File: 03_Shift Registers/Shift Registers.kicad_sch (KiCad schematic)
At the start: 5 parts, among them J1 Data bus, J2 Alu-X bus, J3 Alu-Y bus, J4 Input 1, J5 Input 2

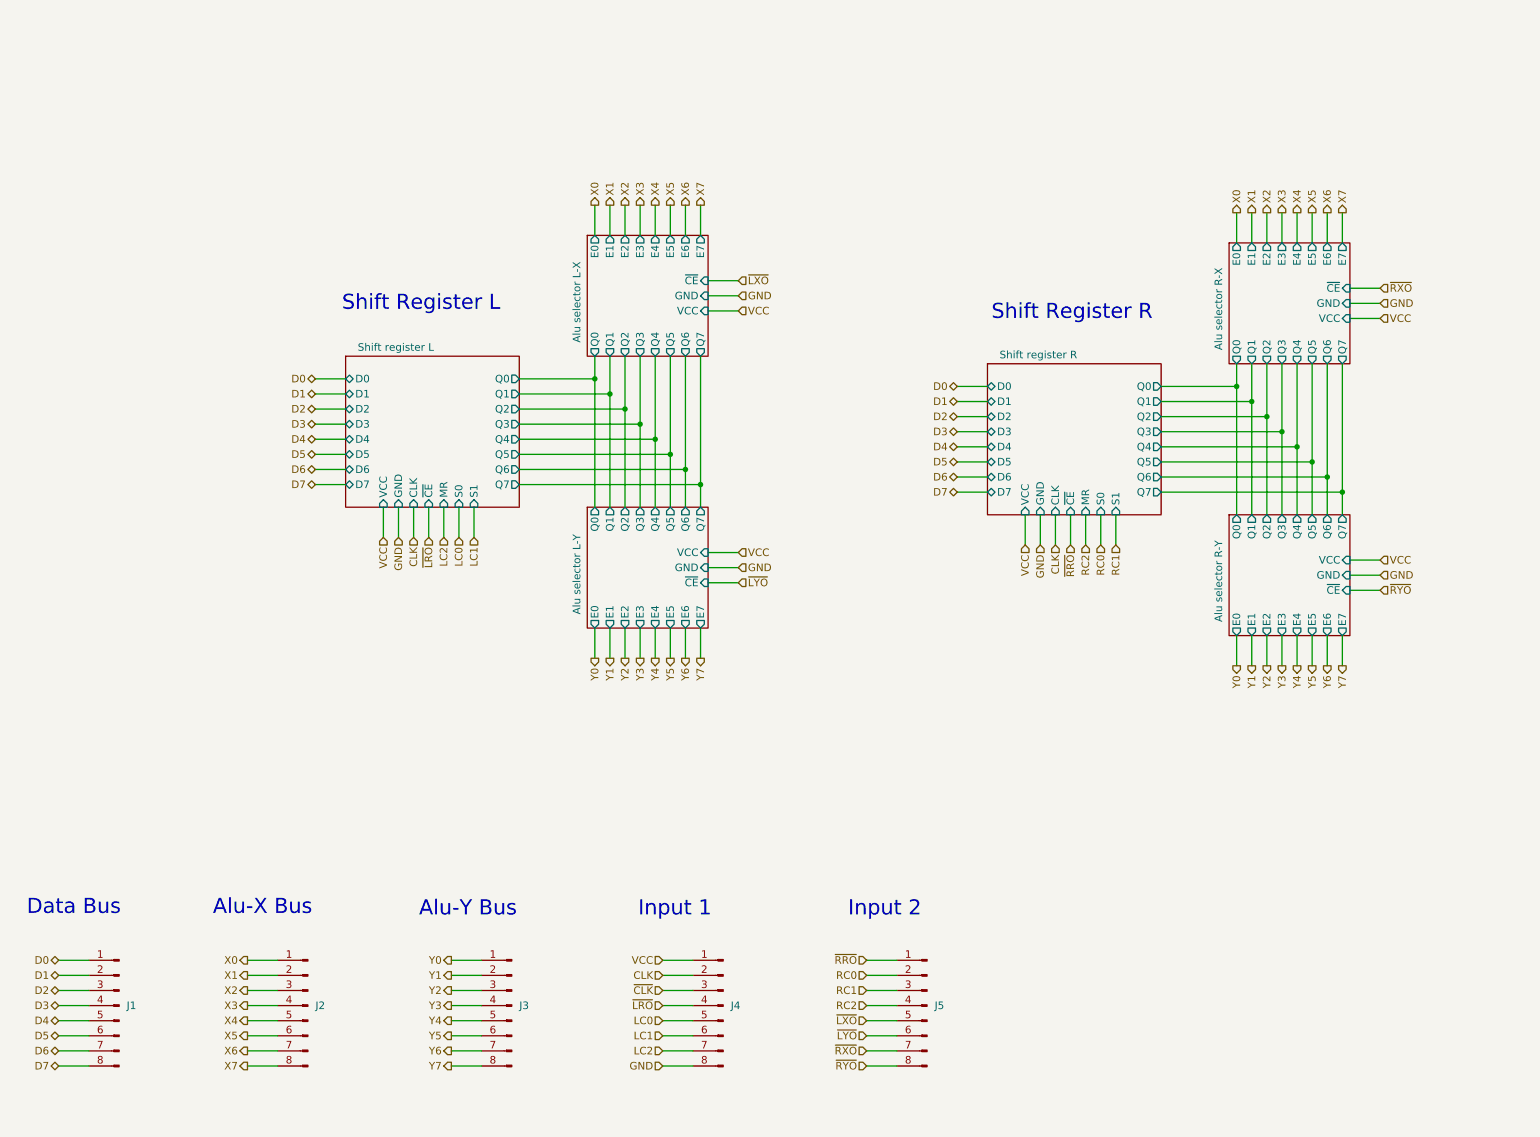
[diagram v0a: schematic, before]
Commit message: Alu control and modules completed, as well as Stack pointer module
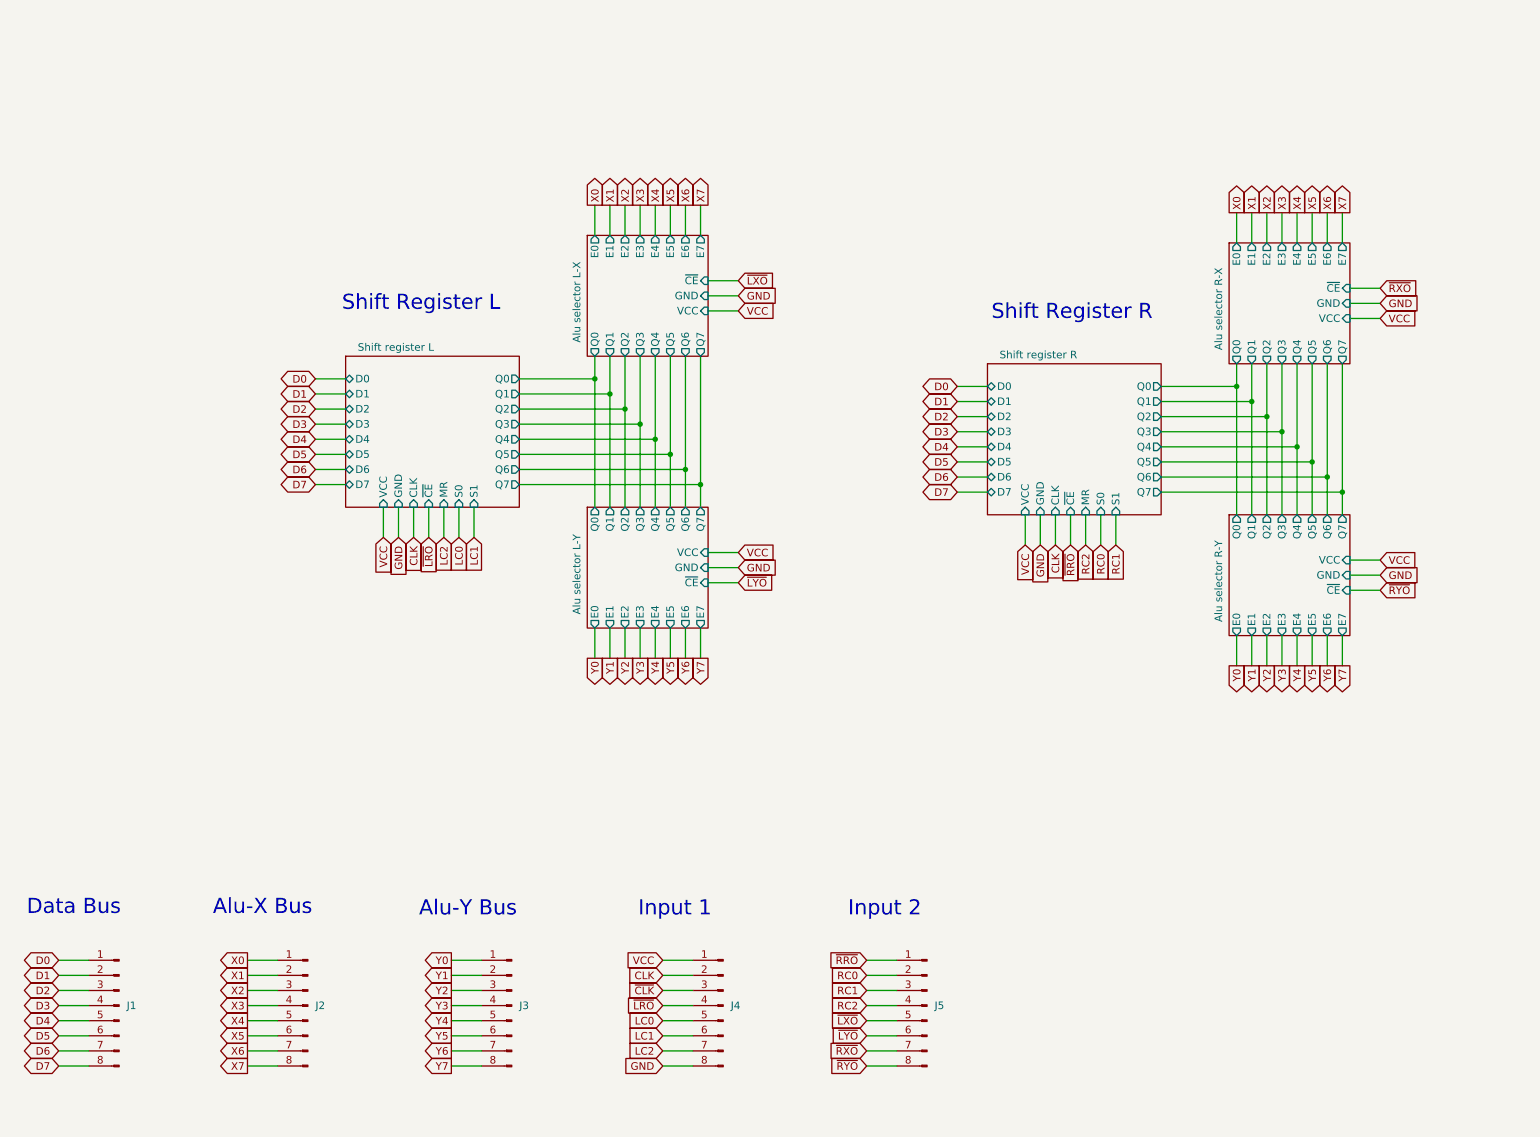
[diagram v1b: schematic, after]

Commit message: Last revision of the cpu, all boards have been ordered. Implementation to be tested and documented in following commits.
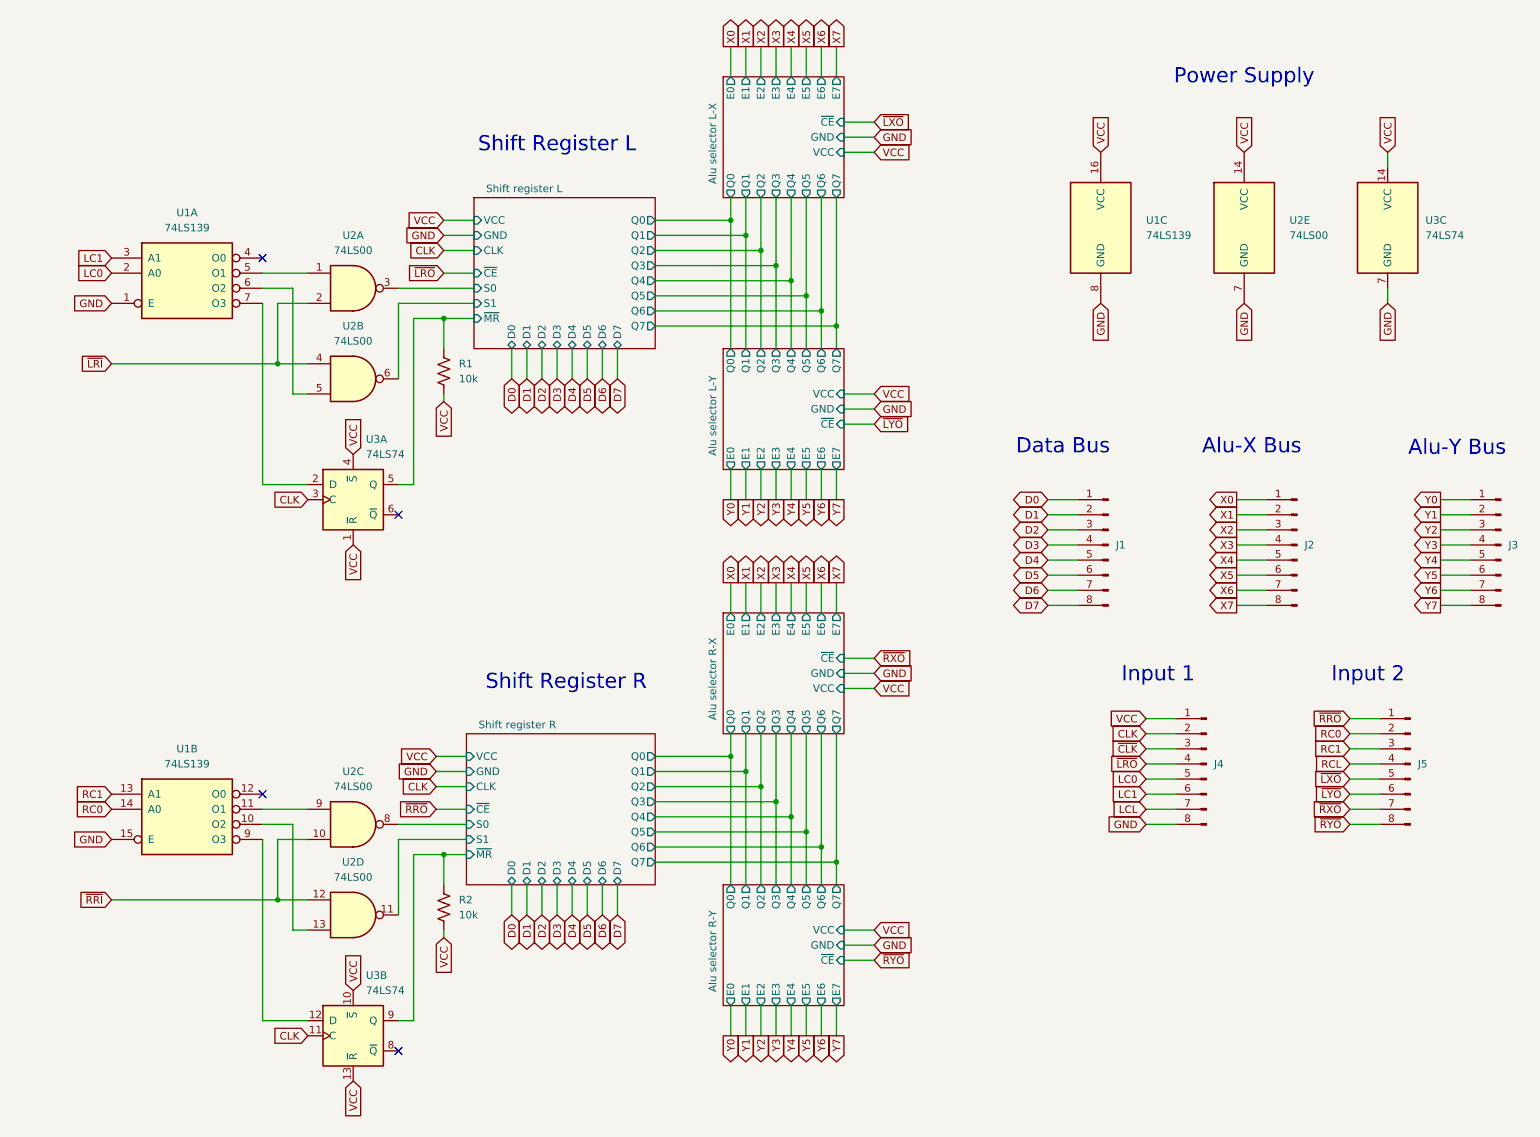
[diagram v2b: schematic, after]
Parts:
- added R1, R2: 10k, symbol Device:R_US
- added U1: 74LS139, Package_DIP:DIP-16_W7.62mm, symbol 74xx:74LS139
- added U2: 74LS00, Package_DIP:DIP-14_W7.62mm, symbol 74xx:74LS00
- added U3: 74LS74, symbol 74xx:74LS74
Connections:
- net CLK: now also U3.11 (C), U3.3 (C)
- net GND: now also U1.1 (E), U1.15 (E), U1.8 (GND), U2.7 (GND), U3.7 (GND)
- net LC0: now also U1.2 (A0)
- net LC1: now also U1.3 (A1)
- net RC0: now also U1.14 (A0)
- net RC1: now also U1.13 (A1)
- net VCC: now also R1.2, R2.2, U1.16 (VCC), U2.14 (VCC), U3.1 (~{R}), U3.10 (~{S}), U3.13 (~{R}), U3.14 (VCC), U3.4 (~{S})
- net LC2 renamed LCL
- net RC2 renamed RCL
- new net: U1.9 (O3), U3.12 (D)
- new net: U1.11 (O1), U2.9
- new net: U1.5 (O1), U2.1
- new net: U1.6 (O2), U2.5
- new net: U1.7 (O3), U3.2 (D)
- new net: U1.10 (O2), U2.13
- new net Shift register L/S0: U2.3
- new net Shift register L/S1: U2.6
- new net Shift register L/~{MR}: R1.1, U3.5 (Q)
- new net Shift register R/S0: U2.8
- new net Shift register R/S1: U2.11
- new net Shift register R/~{MR}: R2.1, U3.9 (Q)
- new net ~{LRI}: U2.2, U2.4
- new net ~{RRI}: U2.10, U2.12
- no-connect marks 0 -> 4
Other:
- sheet Shift register L ports: added ~{MR}; removed MR
- sheet Shift register R ports: added ~{MR}; removed MR
- note added: "Power Supply"
- moved on the sheet: J1, J2, J3, J4, J5
